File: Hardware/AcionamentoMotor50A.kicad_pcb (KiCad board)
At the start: 2 copper layers, 1 part

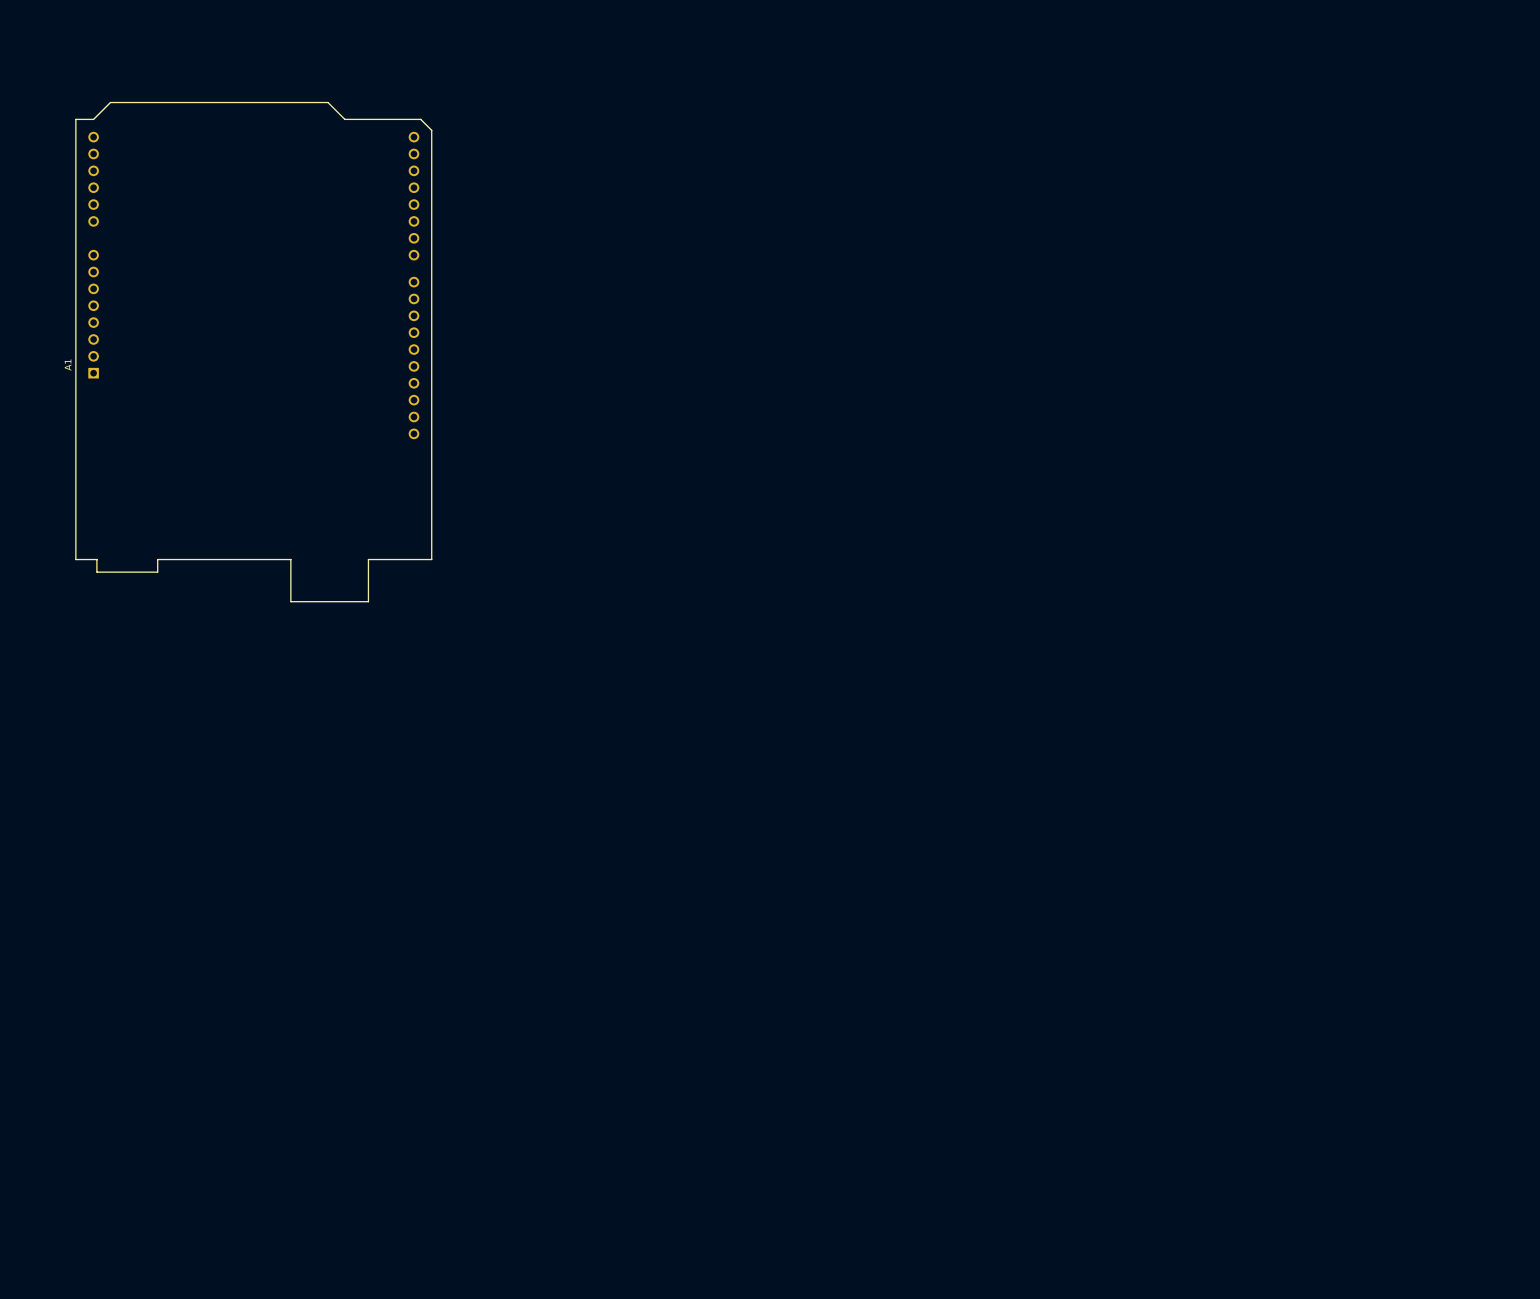
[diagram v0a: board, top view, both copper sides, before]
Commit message: 2026_06_25
Esquemático finalizado.

Footprints corrigidos
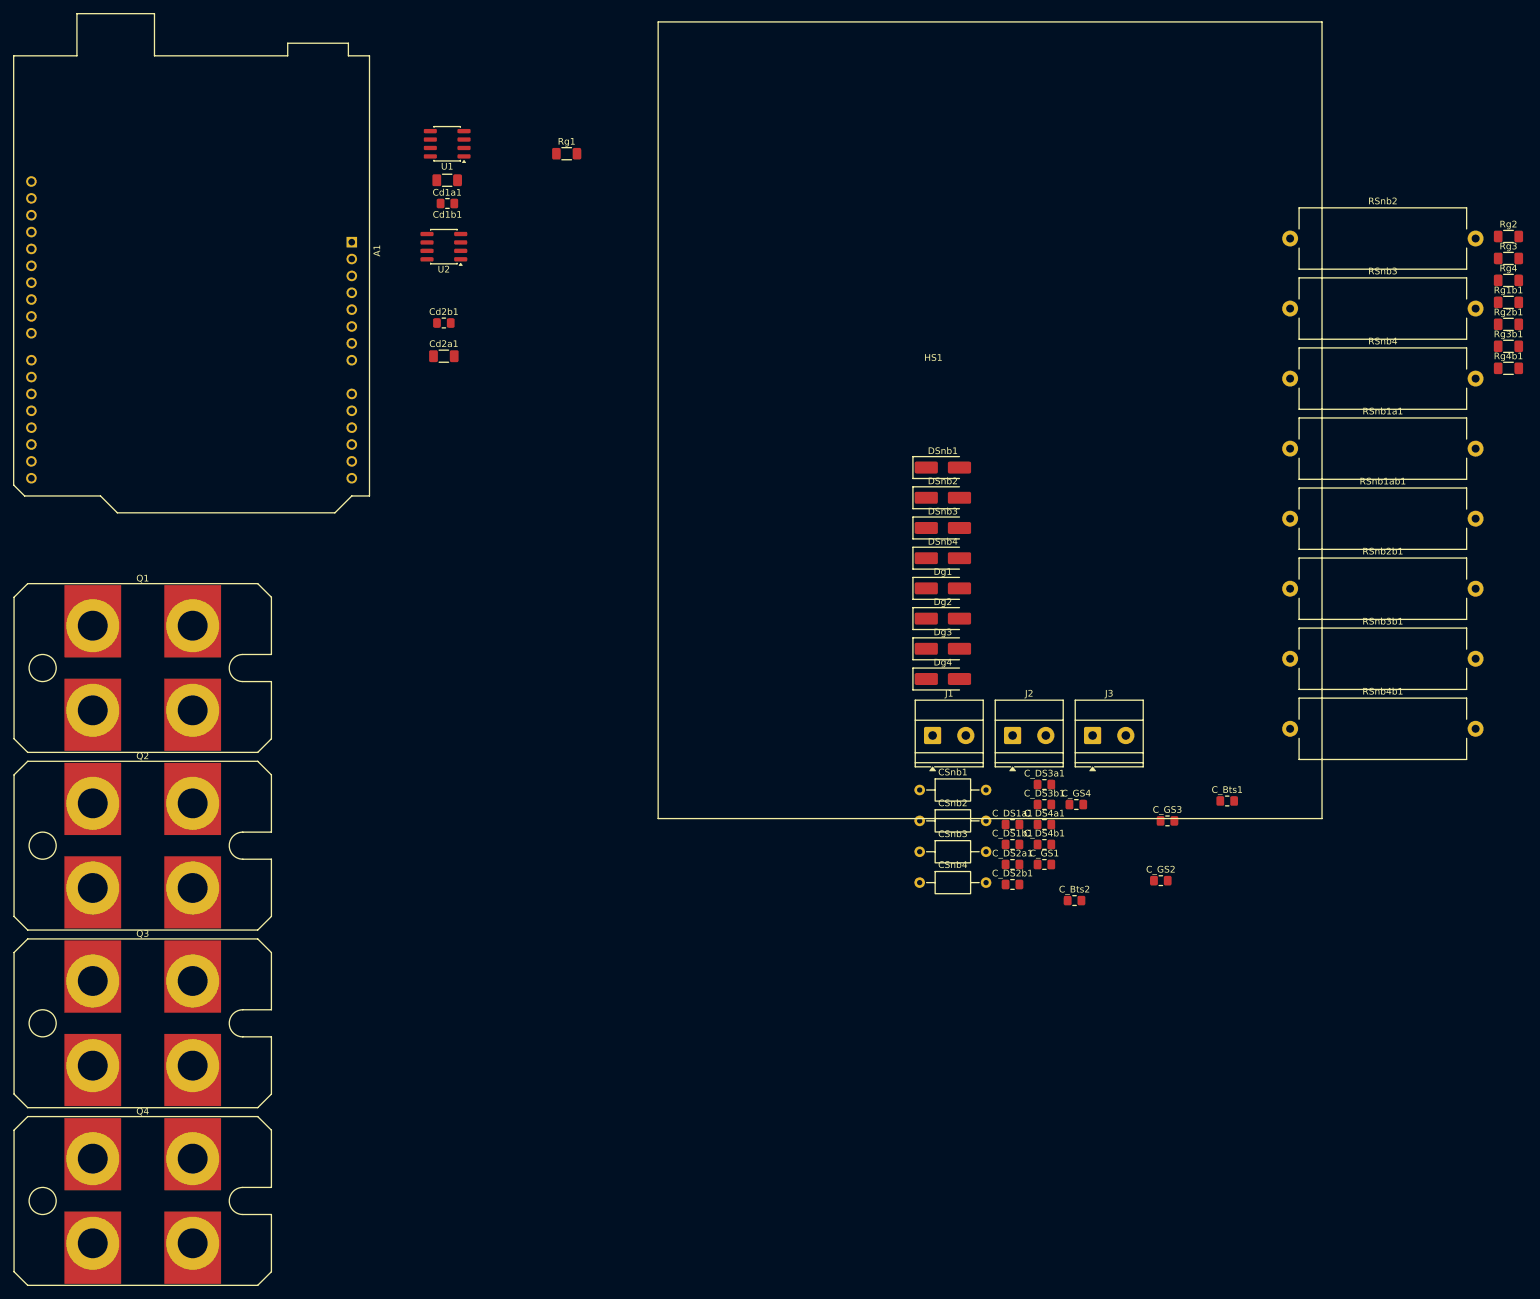
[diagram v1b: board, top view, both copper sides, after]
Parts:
- added CSnb1: 220nF 100V, Capacitor_THT:C_Axial_L5.1mm_D3.1mm_P10.00mm_Horizontal, F.Cu at (168.2, 139.3)
- added CSnb2: 220nF 100V, Capacitor_THT:C_Axial_L5.1mm_D3.1mm_P10.00mm_Horizontal, F.Cu at (168.2, 144.0)
- added CSnb3: 220nF 100V, Capacitor_THT:C_Axial_L5.1mm_D3.1mm_P10.00mm_Horizontal, F.Cu at (168.2, 148.6)
- added CSnb4: 220nF 100V, Capacitor_THT:C_Axial_L5.1mm_D3.1mm_P10.00mm_Horizontal, F.Cu at (168.2, 153.3)
- added C_Bts1: 10uF 50V, Capacitor_SMD:C_0805_2012Metric_Pad1.18x1.45mm_HandSolder, F.Cu at (214.5, 141.0)
- added C_Bts2: 10uF 50V, Capacitor_SMD:C_0805_2012Metric_Pad1.18x1.45mm_HandSolder, F.Cu at (191.5, 156.0)
- added C_DS1a1: 1nF 100V, Capacitor_SMD:C_0805_2012Metric_Pad1.18x1.45mm_HandSolder, F.Cu at (182.2, 144.5)
- added C_DS1b1: 1nF 100V, Capacitor_SMD:C_0805_2012Metric_Pad1.18x1.45mm_HandSolder, F.Cu at (182.2, 147.6)
- added C_DS2a1: 1nF 100V, Capacitor_SMD:C_0805_2012Metric_Pad1.18x1.45mm_HandSolder, F.Cu at (182.2, 150.6)
- added C_DS2b1: 1nF 100V, Capacitor_SMD:C_0805_2012Metric_Pad1.18x1.45mm_HandSolder, F.Cu at (182.2, 153.6)
- added C_DS3a1: 1nF 100V, Capacitor_SMD:C_0805_2012Metric_Pad1.18x1.45mm_HandSolder, F.Cu at (187.0, 138.5)
- added C_DS3b1: 1nF 100V, Capacitor_SMD:C_0805_2012Metric_Pad1.18x1.45mm_HandSolder, F.Cu at (187.0, 141.5)
- added C_DS4a1: 1nF 100V, Capacitor_SMD:C_0805_2012Metric_Pad1.18x1.45mm_HandSolder, F.Cu at (187.0, 144.5)
- added C_DS4b1: 1nF 100V, Capacitor_SMD:C_0805_2012Metric_Pad1.18x1.45mm_HandSolder, F.Cu at (187.0, 147.6)
- added C_GS1: 1nF 100V, Capacitor_SMD:C_0805_2012Metric_Pad1.18x1.45mm_HandSolder, F.Cu at (187.0, 150.6)
- added C_GS2: 1nF 100V, Capacitor_SMD:C_0805_2012Metric_Pad1.18x1.45mm_HandSolder, F.Cu at (204.5, 153.0)
- added C_GS3: 1nF 100V, Capacitor_SMD:C_0805_2012Metric_Pad1.18x1.45mm_HandSolder, F.Cu at (205.5, 144.0)
- added C_GS4: 1nF 100V, Capacitor_SMD:C_0805_2012Metric_Pad1.18x1.45mm_HandSolder, F.Cu at (191.8, 141.5)
- added Cd1a1: 1uF, Capacitor_SMD:C_1206_3216Metric_Pad1.33x1.80mm_HandSolder, F.Cu at (97.0, 47.5)
- added Cd1b1: 100nF, Capacitor_SMD:C_0805_2012Metric_Pad1.18x1.45mm_HandSolder, F.Cu at (97.0, 51.0)
- added Cd2a1: 1uF, Capacitor_SMD:C_1206_3216Metric_Pad1.33x1.80mm_HandSolder, F.Cu at (96.5, 74.0)
- added Cd2b1: 100nF, Capacitor_SMD:C_0805_2012Metric_Pad1.18x1.45mm_HandSolder, F.Cu at (96.5, 69.0)
- added DSnb1: D, Diode_SMD:D_SMA_Handsoldering, F.Cu at (171.7, 90.8)
- added DSnb2: D, Diode_SMD:D_SMA_Handsoldering, F.Cu at (171.7, 95.3)
- added DSnb3: D, Diode_SMD:D_SMA_Handsoldering, F.Cu at (171.7, 99.9)
- added DSnb4: D, Diode_SMD:D_SMA_Handsoldering, F.Cu at (171.7, 104.4)
- added Dg1: ES3B, Diode_SMD:D_SMA_Handsoldering, F.Cu at (171.7, 109.0)
- added Dg2: ES3B, Diode_SMD:D_SMA_Handsoldering, F.Cu at (171.7, 113.5)
- added Dg3: ES3B, Diode_SMD:D_SMA_Handsoldering, F.Cu at (171.7, 118.1)
- added Dg4: ES3B, Diode_SMD:D_SMA_Handsoldering, F.Cu at (171.7, 122.6)
- added HS1: Heatsink, ZeniteSolar:Heatsink_120mmx100mm_H70mm, F.Cu at (178.8, 83.7)
- added J1: Conn_01x02, TerminalBlock_Phoenix:TerminalBlock_Phoenix_MKDS-1,5-2_1x02_P5.00mm_Horizontal, F.Cu at (170.1, 131.1)
- added J2: Conn_01x02, TerminalBlock_Phoenix:TerminalBlock_Phoenix_MKDS-1,5-2_1x02_P5.00mm_Horizontal, F.Cu at (182.2, 131.1)
- added J3: Conn_01x02, TerminalBlock_Phoenix:TerminalBlock_Phoenix_MKDS-1,5-2_1x02_P5.00mm_Horizontal, F.Cu at (194.2, 131.1)
- added Q1: IXFN420N10T, ZeniteSolar:SOT-227, F.Cu at (43.6, 114.6)
- added Q2: IXFN420N10T, ZeniteSolar:SOT-227, F.Cu at (43.6, 141.4)
- added Q3: IXFN420N10T, ZeniteSolar:SOT-227, F.Cu at (43.6, 168.1)
- added Q4: IXFN420N10T, ZeniteSolar:SOT-227, F.Cu at (43.6, 194.9)
- added RSnb1a1: 3K3 5W, Resistor_THT:R_Axial_Power_L25.0mm_W9.0mm_P27.94mm, F.Cu at (224.0, 87.9)
- added RSnb1ab1: 3K3 5W, Resistor_THT:R_Axial_Power_L25.0mm_W9.0mm_P27.94mm, F.Cu at (224.0, 98.5)
- added RSnb2: 3K3 5W, Resistor_THT:R_Axial_Power_L25.0mm_W9.0mm_P27.94mm, F.Cu at (224.0, 56.3)
- added RSnb2b1: 3K3 5W, Resistor_THT:R_Axial_Power_L25.0mm_W9.0mm_P27.94mm, F.Cu at (224.0, 109.0)
- added RSnb3: 3K3 5W, Resistor_THT:R_Axial_Power_L25.0mm_W9.0mm_P27.94mm, F.Cu at (224.0, 66.8)
- added RSnb3b1: 3K3 5W, Resistor_THT:R_Axial_Power_L25.0mm_W9.0mm_P27.94mm, F.Cu at (224.0, 119.6)
- added RSnb4: 3K3 5W, Resistor_THT:R_Axial_Power_L25.0mm_W9.0mm_P27.94mm, F.Cu at (224.0, 77.4)
- added RSnb4b1: 3K3 5W, Resistor_THT:R_Axial_Power_L25.0mm_W9.0mm_P27.94mm, F.Cu at (224.0, 130.1)
- added Rg1: 3R, Resistor_SMD:R_1206_3216Metric_Pad1.30x1.75mm_HandSolder, F.Cu at (115.0, 43.5)
- added Rg1b1: 3R, Resistor_SMD:R_1206_3216Metric_Pad1.30x1.75mm_HandSolder, F.Cu at (256.9, 65.9)
- added Rg2: 3R, Resistor_SMD:R_1206_3216Metric_Pad1.30x1.75mm_HandSolder, F.Cu at (256.9, 56.0)
- added Rg2b1: 3R, Resistor_SMD:R_1206_3216Metric_Pad1.30x1.75mm_HandSolder, F.Cu at (256.9, 69.2)
- added Rg3: 3R, Resistor_SMD:R_1206_3216Metric_Pad1.30x1.75mm_HandSolder, F.Cu at (256.9, 59.3)
- added Rg3b1: 3R, Resistor_SMD:R_1206_3216Metric_Pad1.30x1.75mm_HandSolder, F.Cu at (256.9, 72.5)
- added Rg4: 3R, Resistor_SMD:R_1206_3216Metric_Pad1.30x1.75mm_HandSolder, F.Cu at (256.9, 62.6)
- added Rg4b1: 3R, Resistor_SMD:R_1206_3216Metric_Pad1.30x1.75mm_HandSolder, F.Cu at (256.9, 75.8)
- added U1: MP1923, Package_SO:SOP-8_3.76x4.96mm_P1.27mm, F.Cu at (97.0, 42.0)
- added U2: MP1923, Package_SO:SOP-8_3.76x4.96mm_P1.27mm, F.Cu at (96.5, 57.5)
- moved A1 43.6 mm to (82.6, 56.8), turned to -90 degrees
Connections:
- A1 pad 29: unconnected-(A1-GND-Pad29) -> GNDREF
- A1 pad 6: unconnected-(A1-GND-Pad6) -> GNDREF
- A1 pad 7: unconnected-(A1-GND-Pad7) -> GNDREF
